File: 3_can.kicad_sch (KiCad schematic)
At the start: 6 parts, among them J301 Conn_01x04_Male, U301 TJA1441AT

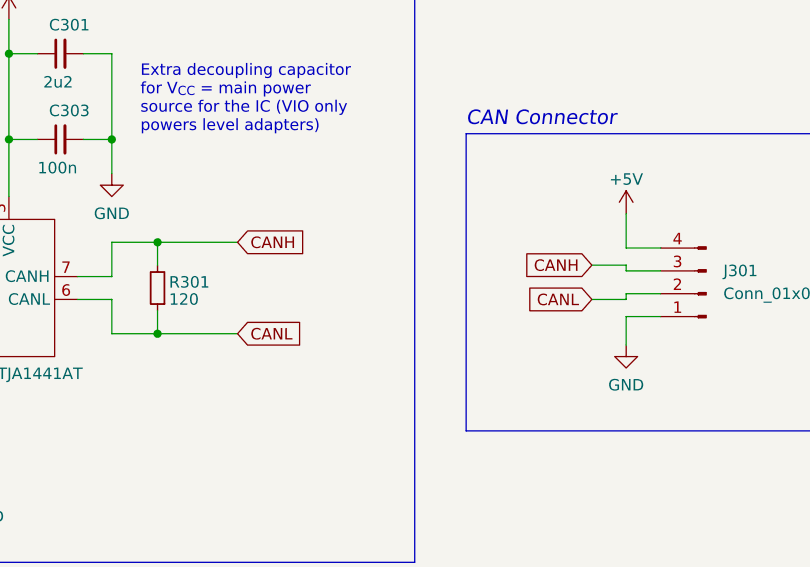
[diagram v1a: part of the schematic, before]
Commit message: global labels to local labels wherever possible and mcu pinout addition
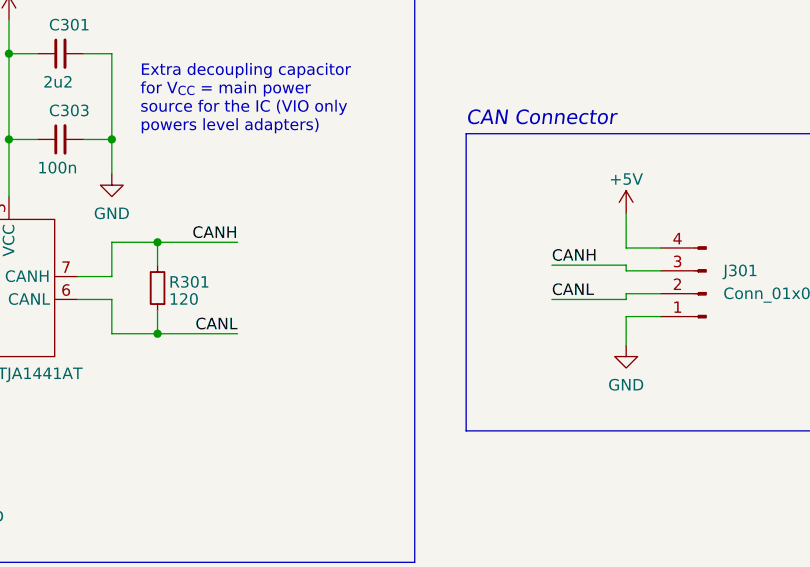
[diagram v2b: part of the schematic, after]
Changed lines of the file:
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@@
     (stroke (width 0) (type default))
   )
-  (wire (pts (xy 196.215 102.87) (xy 200.025 102.87))
+  (wire (pts (xy 191.77 102.87) (xy 200.025 102.87))
     (stroke (width 0) (type default))
   )
@@
     (stroke (width 0) (type default))
   )
-  (wire (pts (xy 196.215 99.06) (xy 200.025 99.06))
+  (wire (pts (xy 191.77 99.06) (xy 200.025 99.06))
     (stroke (width 0) (type default))
   )
@@
     (effects (font (size 3.5 3.5) (thickness 0.8) bold) (justify left bottom))
   )
-  (global_label "CANL" (shape input) (at 156.845 106.68 0) (fields_autoplaced)
-    (effects (font (size 1.27 1.27)) (justify left))
-    (property "Intersheetrefs" "${INTERSHEET_REFS}" (at 163.9752 106.6006 0)
-      (effects (font (size 1.27 1.27)) (justify left) hide)
-    )
+  (label "CANL" (at 156.845 106.68 180) (fields_autoplaced)
+    (effects (font (size 1.27 1.27)) (justify right bottom))
   )
-  (global_label "CANH" (shape input) (at 156.845 96.52 0) (fields_autoplaced)
-    (effects (font (size 1.27 1.27)) (justify left))
-    (property "Intersheetrefs" "${INTERSHEET_REFS}" (at 164.2776 96.4406 0)
-      (effects (font (size 1.27 1.27)) (justify left) hide)
-    )
+  (label "CANH" (at 156.845 96.52 180) (fields_autoplaced)
+    (effects (font (size 1.27 1.27)) (justify right bottom))
   )
-  (global_label "CANH" (shape input) (at 196.215 99.06 180) (fields_autoplaced)
-    (effects (font (size 1.27 1.27)) (justify right))
-    (property "Intersheetrefs" "${INTERSHEET_REFS}" (at 188.7824 99.1394 0)
-      (effects (font (size 1.27 1.27)) (justify right) hide)
-    )
+  (label "CANL" (at 191.77 102.87 0) (fields_autoplaced)
+    (effects (font (size 1.27 1.27)) (justify left bottom))
+  )
+  (label "CANH" (at 191.77 99.06 0) (fields_autoplaced)
+    (effects (font (size 1.27 1.27)) (justify left bottom))
   )
   (global_label "CAN_RXD" (shape input) (at 109.22 104.14 180) (fields_autoplaced)
@@
       (effects (font (size 1.27 1.27)) (justify right) hide)
     )
-  )
-  (global_label "CANL" (shape input) (at 196.215 102.87 180) (fields_autoplaced)
-    (effects (font (size 1.27 1.27)) (justify right))
-    (property "Intersheetrefs" "${INTERSHEET_REFS}" (at 189.0848 102.9494 0)
-      (effects (font (size 1.27 1.27)) (justify right) hide)
-    )

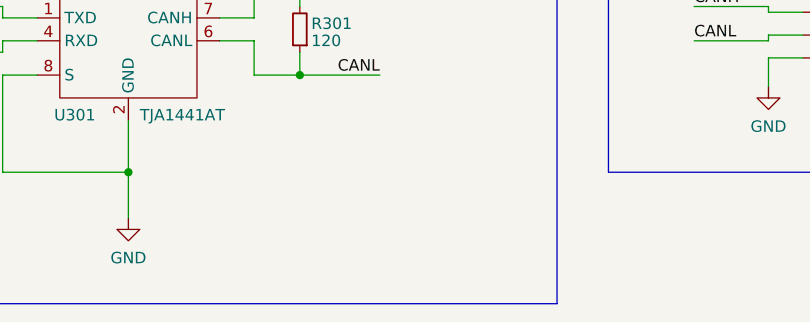
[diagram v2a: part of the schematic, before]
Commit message: check ESD protection for CAN and SWD bus
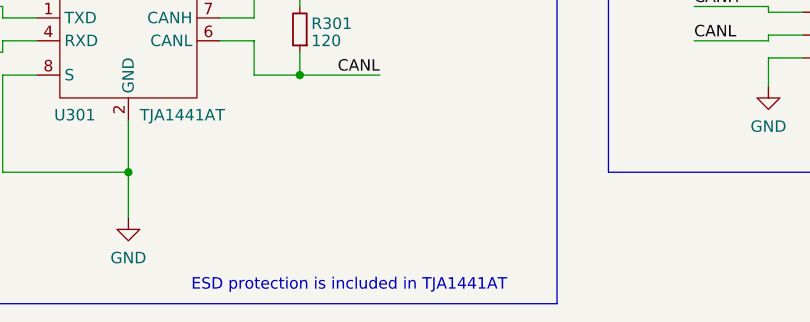
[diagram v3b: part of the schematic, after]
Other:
- note added: "ESD protection is included in TJA1441AT"
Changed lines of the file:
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@@
     (effects (font (size 1.6 1.6) italic) (justify left bottom))
+  )
+  (text "ESD protection is included in TJA1441AT" (at 135.89 130.81 0)
+    (effects (font (size 1.27 1.27)) (justify left bottom))
   )
   (text "[3] CAN" (at 18.415 25.4 0)

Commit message: feat: new phases, LED pins
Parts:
- R301: footprint Resistor_SMD:R_0402_1005Metric_Pad0.72x0.64mm_HandSolder -> Resistor_SMD:R_0603_1608Metric_Pad0.98x0.95mm_HandSolder
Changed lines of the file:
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@@
       (effects (font (size 1.27 1.27)) (justify right))
     )
-    (property "Footprint" "Resistor_SMD:R_0402_1005Metric_Pad0.72x0.64mm_HandSolder" (at 147.955 101.6 0)
+    (property "Footprint" "Resistor_SMD:R_0603_1608Metric_Pad0.98x0.95mm_HandSolder" (at 147.955 101.6 0)
       (effects (font (size 1.27 1.27)) hide)
     )

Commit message: feat: LED routing, encoder interface, footprint updates
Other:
- title: CAN [3] -> CAN
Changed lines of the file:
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@@
   (paper "A4")
   (title_block
-    (title "CAN [3]")
-    (date "2023-04-16")
+    (title "CAN")
+    (date "2023-11-25")
     (rev "1.0")
   )
@@
   (symbol (lib_id "power:GND") (at 114.935 88.9 0) (unit 1)
     (in_bom yes) (on_board yes) (dnp no)
-    (property "Reference" "#PWR?" (at 114.935 95.25 0)
+    (property "Reference" "#PWR0139" (at 114.935 95.25 0)
       (effects (font (size 1.27 1.27)) hide)
     )
@@
       (project "ESC_R1"
         (path "/9dea2e18-5867-4ed4-a12d-7ee109225de0/b6b0d34a-9e25-4b05-9733-a3c9d6720b5f"
-          (reference "#PWR?") (unit 1)
+          (reference "#PWR0139") (unit 1)
         )
         (path "/9dea2e18-5867-4ed4-a12d-7ee109225de0/4b568fb1-3ffb-4d91-93b3-473275569108"
@@
   (symbol (lib_id "power:+5V") (at 200.025 93.345 0) (unit 1)
     (in_bom yes) (on_board yes) (dnp no)
-    (property "Reference" "#PWR?" (at 200.025 97.155 0)
+    (property "Reference" "#PWR0136" (at 200.025 97.155 0)
       (effects (font (size 1.27 1.27)) hide)
     )
@@
       (project "ESC_R1"
         (path "/9dea2e18-5867-4ed4-a12d-7ee109225de0/b6b0d34a-9e25-4b05-9733-a3c9d6720b5f"
-          (reference "#PWR?") (unit 1)
+          (reference "#PWR0136") (unit 1)
         )
         (path "/9dea2e18-5867-4ed4-a12d-7ee109225de0/4b568fb1-3ffb-4d91-93b3-473275569108"
@@
   (symbol (lib_id "power:GND") (at 128.905 122.555 0) (unit 1)
     (in_bom yes) (on_board yes) (dnp no)
-    (property "Reference" "#PWR?" (at 128.905 128.905 0)
+    (property "Reference" "#PWR0142" (at 128.905 128.905 0)
       (effects (font (size 1.27 1.27)) hide)
     )
@@
       (project "ESC_R1"
         (path "/9dea2e18-5867-4ed4-a12d-7ee109225de0/b6b0d34a-9e25-4b05-9733-a3c9d6720b5f"
-          (reference "#PWR?") (unit 1)
+          (reference "#PWR0142") (unit 1)
         )
         (path "/9dea2e18-5867-4ed4-a12d-7ee109225de0/4b568fb1-3ffb-4d91-93b3-473275569108"
@@
   (symbol (lib_id "power:+5V") (at 131.445 71.755 0) (unit 1)
     (in_bom yes) (on_board yes) (dnp no)
-    (property "Reference" "#PWR?" (at 131.445 75.565 0)
+    (property "Reference" "#PWR0140" (at 131.445 75.565 0)
       (effects (font (size 1.27 1.27)) hide)
     )
@@
       (project "ESC_R1"
         (path "/9dea2e18-5867-4ed4-a12d-7ee109225de0/b6b0d34a-9e25-4b05-9733-a3c9d6720b5f"
-          (reference "#PWR?") (unit 1)
+          (reference "#PWR0140") (unit 1)
         )
         (path "/9dea2e18-5867-4ed4-a12d-7ee109225de0/4b568fb1-3ffb-4d91-93b3-473275569108"
@@
   (symbol (lib_id "power:+3.3V") (at 126.365 80.645 0) (unit 1)
     (in_bom yes) (on_board yes) (dnp no)
-    (property "Reference" "#PWR?" (at 126.365 84.455 0)
+    (property "Reference" "#PWR0141" (at 126.365 84.455 0)
       (effects (font (size 1.27 1.27)) hide)
     )
@@
       (project "ESC_R1"
         (path "/9dea2e18-5867-4ed4-a12d-7ee109225de0/b6b0d34a-9e25-4b05-9733-a3c9d6720b5f"
-          (reference "#PWR?") (unit 1)
+          (reference "#PWR0141") (unit 1)
         )
         (path "/9dea2e18-5867-4ed4-a12d-7ee109225de0/4b568fb1-3ffb-4d91-93b3-473275569108"
@@
   (symbol (lib_id "power:GND") (at 142.875 88.9 0) (mirror y) (unit 1)
     (in_bom yes) (on_board yes) (dnp no)
-    (property "Reference" "#PWR?" (at 142.875 95.25 0)
+    (property "Reference" "#PWR0138" (at 142.875 95.25 0)
       (effects (font (size 1.27 1.27)) hide)
     )
@@
       (project "ESC_R1"
         (path "/9dea2e18-5867-4ed4-a12d-7ee109225de0/b6b0d34a-9e25-4b05-9733-a3c9d6720b5f"
-          (reference "#PWR?") (unit 1)
+          (reference "#PWR0138") (unit 1)
         )
         (path "/9dea2e18-5867-4ed4-a12d-7ee109225de0/4b568fb1-3ffb-4d91-93b3-473275569108"
@@
   (symbol (lib_id "power:GND") (at 200.025 107.95 0) (unit 1)
     (in_bom yes) (on_board yes) (dnp no)
-    (property "Reference" "#PWR?" (at 200.025 114.3 0)
+    (property "Reference" "#PWR0137" (at 200.025 114.3 0)
       (effects (font (size 1.27 1.27)) hide)
     )
@@
       (project "ESC_R1"
         (path "/9dea2e18-5867-4ed4-a12d-7ee109225de0/b6b0d34a-9e25-4b05-9733-a3c9d6720b5f"
-          (reference "#PWR?") (unit 1)
-        )
-        (path "/9dea2e18-5867-4ed4-a12d-7ee109225de0/4b568fb1-3ffb-4d91-93b3-473275569108"
+          (reference "#PWR0137") (unit 1)
+        )
+        (path "/9dea2e18-5867-4ed4-a12d-7ee109225de0/4b568fb1-3ffb-4d91-93b3-473275569108"

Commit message: feat: footprint assignment, circuit check and routing kickoff
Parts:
- J301: footprint (none) -> Connector_PinHeader_2.54mm:PinHeader_1x04_P2.54mm_Vertical
- U301: Link (none) -> https://www.mouser.de/ProductDetail/NXP-Semiconductors/TJA1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
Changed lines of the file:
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@@
   (title_block
     (title "CAN")
-    (date "2023-11-25")
+    (date "2023-11-26")
     (rev "1.0")
   )
@@
       (effects (font (size 1.27 1.27)) (justify right))
     )
-    (property "Footprint" "" (at 208.915 102.235 0)
+    (property "Footprint" "Connector_PinHeader_2.54mm:PinHeader_1x04_P2.54mm_Vertical" (at 208.915 102.235 0)
       (effects (font (size 1.27 1.27)) hide)
     )
@@
       (effects (font (size 1.27 1.27)) hide)
     )
+    (property "Link" "https://www.mouser.de/ProductDetail/NXP-Semiconductors/TJA1441AT-0Z?qs=eP2BKZSCXI7fcqmlBnmIFw%3D%3D" (at 128.905 101.6 0)
+      (effects (font (size 1.27 1.27)) hide)
+    )

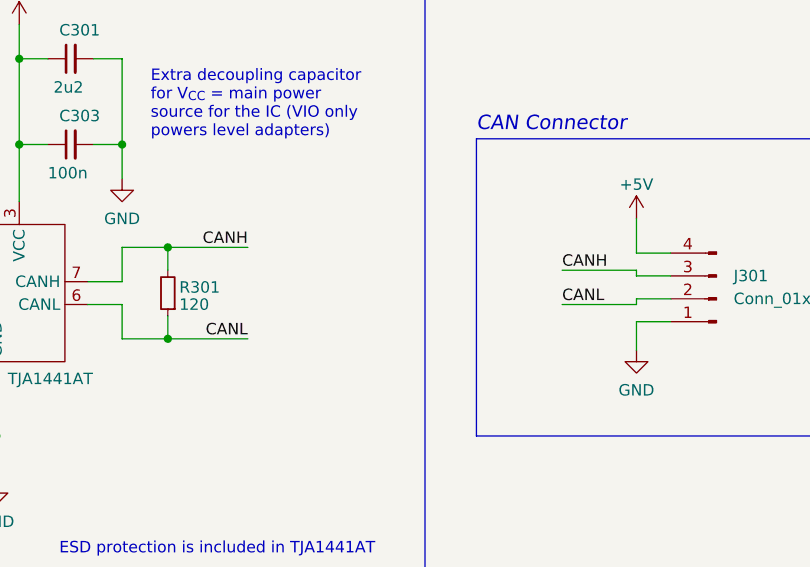
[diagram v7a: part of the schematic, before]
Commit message: feat: single phase, HSE, CAN routing and general layout
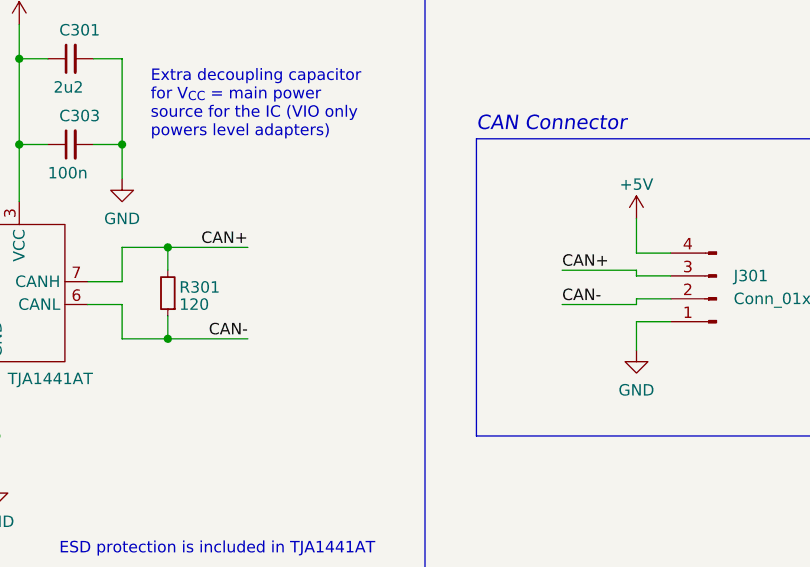
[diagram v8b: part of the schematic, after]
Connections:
- net CANH renamed CAN+
- net CANL renamed CAN-
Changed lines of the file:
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@@
     (effects (font (size 3.5 3.5) (thickness 0.8) bold) (justify left bottom))
   )
-  (label "CANL" (at 156.845 106.68 180) (fields_autoplaced)
+  (label "CAN-" (at 156.845 106.68 180) (fields_autoplaced)
     (effects (font (size 1.27 1.27)) (justify right bottom))
   )
-  (label "CANH" (at 156.845 96.52 180) (fields_autoplaced)
+  (label "CAN+" (at 156.845 96.52 180) (fields_autoplaced)
     (effects (font (size 1.27 1.27)) (justify right bottom))
   )
-  (label "CANL" (at 191.77 102.87 0) (fields_autoplaced)
+  (label "CAN-" (at 191.77 102.87 0) (fields_autoplaced)
     (effects (font (size 1.27 1.27)) (justify left bottom))
   )
-  (label "CANH" (at 191.77 99.06 0) (fields_autoplaced)
+  (label "CAN+" (at 191.77 99.06 0) (fields_autoplaced)
     (effects (font (size 1.27 1.27)) (justify left bottom))
   )
